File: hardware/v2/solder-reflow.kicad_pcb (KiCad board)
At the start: 2 copper layers, 108 parts, among them J1 USB_C_Receptacle_USB2.0_14P, J11 I2C, J13 RTD_PT100, J14 SSROUT2, J15 LCD_CONN, J16 UART, J17 USB_C_Receptacle_USB2.0_14P, J2 I2S, J3 PINOUT, J4 220V, J5 HEATER, J6 InputButton, J7 PINOUT, J8 PINOUT, J9 12VIN, K1 G3MB202PDC12, Q1 SS8550, Q2 SS8550, Q3 SS8050, Q4 SS8050, SW1 L, SW2 RST, SW3 SWH11AA1, SW4 D, SW5 U, SW6 R, SW7 R, SW8 R, SW9 Boot, U3 L7805, U4 AMS1117-3.3, U5 ESP32-S3-WROOM-1, U6 74LS14, U7 H11AA1, U8 CH340C, U9 MAX31865xTP

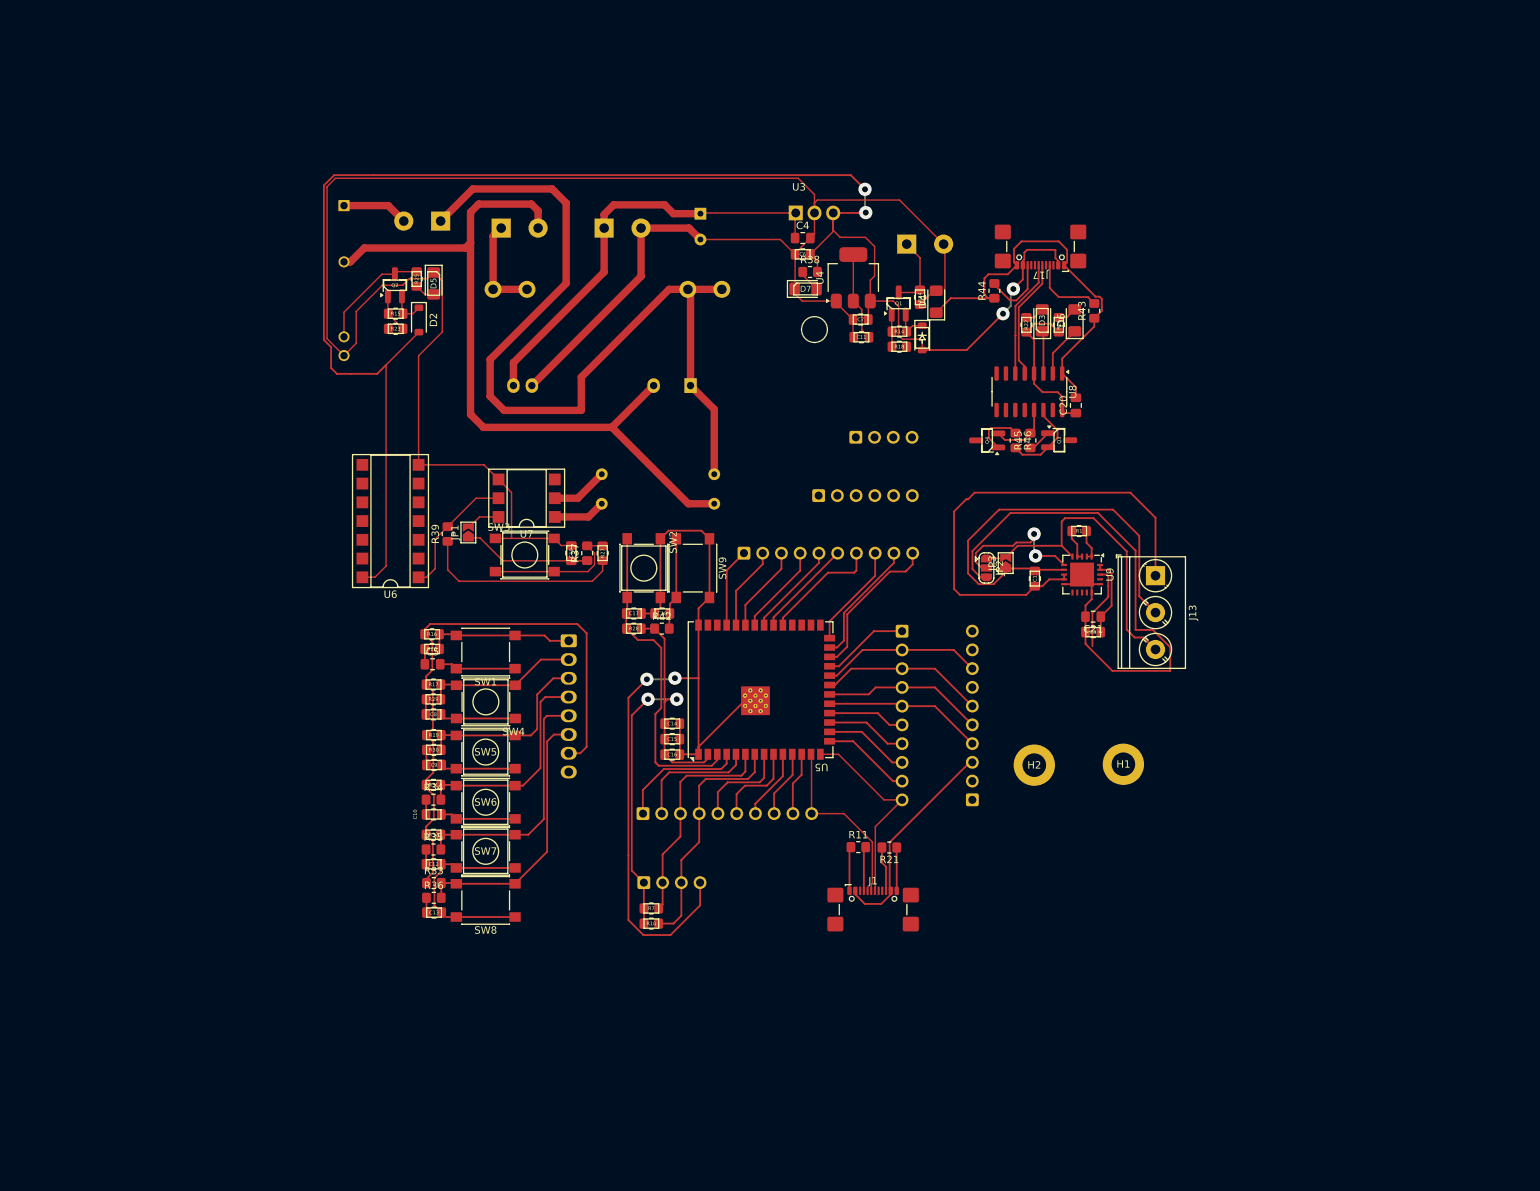
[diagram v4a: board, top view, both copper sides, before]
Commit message: feat: change to use esp32-s3 tempel
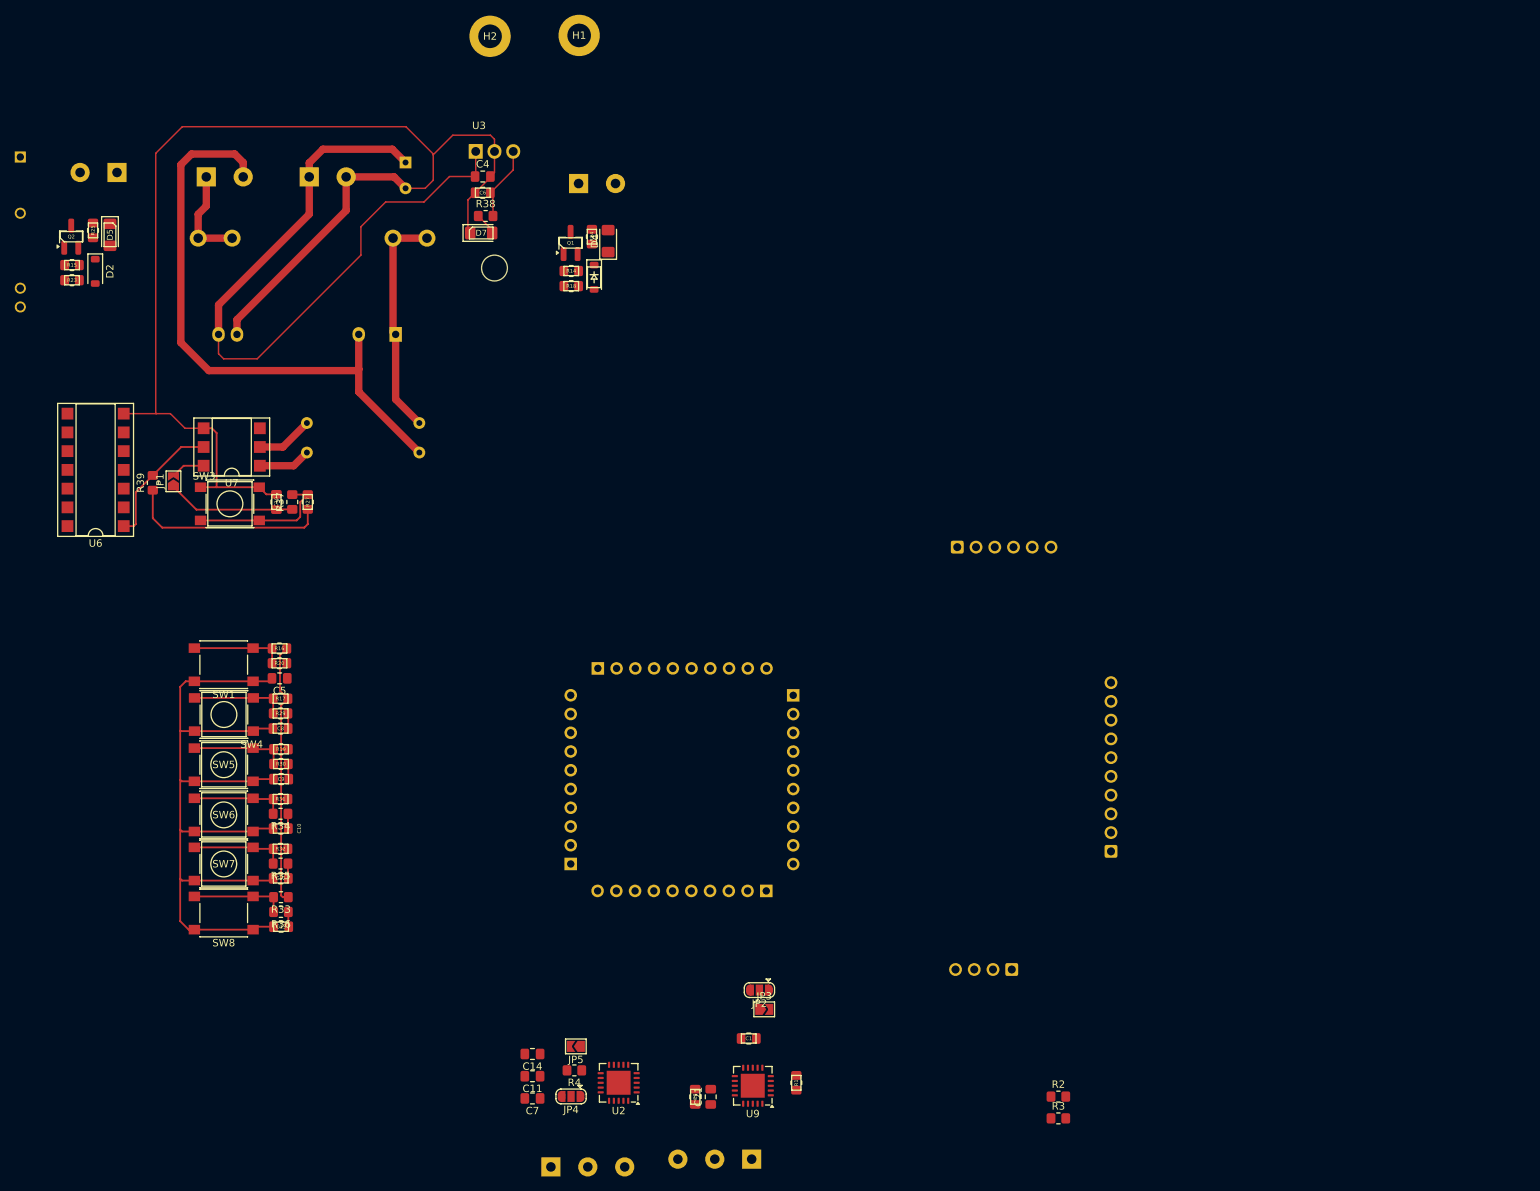
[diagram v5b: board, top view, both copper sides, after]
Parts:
- removed C15: 22uF, Capacitor_SMD:C_0805_2012Metric_Pad1.18x1.45mm_HandSolder
- removed C16: 1uF, Capacitor_SMD:C_0805_2012Metric_Pad1.18x1.45mm_HandSolder
- removed C17, C18, C20: 100nF, Capacitor_SMD:C_0805_2012Metric_Pad1.18x1.45mm_HandSolder
- removed D3: TXD, LED_SMD:LED_1206_3216Metric_Pad1.42x1.75mm_HandSolder
- removed D6: RXD, LED_SMD:LED_1206_3216Metric_Pad1.42x1.75mm_HandSolder
- removed J11: I2C, Connector_Molex:Molex_SL_171971-0004_1x04_P2.54mm_Vertical
- removed J16: UART, Connector_Molex:Molex_SL_171971-0004_1x04_P2.54mm_Vertical
- removed J17: USB_C_Receptacle_USB2.0_14P, Connector_USB:USB_C_Receptacle_GCT_USB4110
- removed J6: InputButton, Connector_Molex:Molex_KK-254_AE-6410-08A_1x08_P2.54mm_Vertical
- removed J7, J8: PINOUT, Connector_Molex:Molex_SL_171971-0010_1x10_P2.54mm_Vertical
- removed Q3, Q4: SS8050, Package_TO_SOT_SMD:SOT-23_Handsoldering
- removed R10, R7: 4K7, Resistor_SMD:R_0805_2012Metric_Pad1.20x1.40mm_HandSolder
- removed R11, R21, R43, R44: 5K1, Resistor_SMD:R_0805_2012Metric_Pad1.20x1.40mm_HandSolder
- removed R22, R26, R28, R42: 1k, Resistor_SMD:R_0805_2012Metric_Pad1.20x1.40mm_HandSolder
- removed R45, R46: 10k, Resistor_SMD:R_0805_2012Metric_Pad1.20x1.40mm_HandSolder
- removed SW2: RST, Button_Switch_SMD:SW_Push_1P1T_NO_6x6mm_H9.5mm
- removed SW9: Boot, Button_Switch_SMD:SW_Push_1P1T_NO_6x6mm_H9.5mm
- removed U4: AMS1117-3.3, Package_TO_SOT_SMD:SOT-223-3_TabPin2
- removed U5: ESP32-S3-WROOM-1, RF_Module:ESP32-S3-WROOM-1U
- removed U8: CH340C, Package_SO:SOIC-16_3.9x9.9mm_P1.27mm
- added JP4: 3_OR_2_Wire, Jumper:SolderJumper-3_P1.3mm_Open_RoundedPad1.0x1.5mm, F.Cu at (102.6, 164.9)
- added JP5: 2_Wire, Jumper:SolderJumper-2_P1.3mm_Open_TrianglePad1.0x1.5mm, F.Cu at (103.3, 158.1)
- added R2: 4K7, Resistor_SMD:R_0805_2012Metric_Pad1.20x1.40mm_HandSolder, F.Cu at (168.6, 164.9)
- added R3: 4K7, Resistor_SMD:R_0805_2012Metric_Pad1.20x1.40mm_HandSolder, F.Cu at (168.6, 167.8)
- added R4: 400 1%, Resistor_SMD:R_0805_2012Metric_Pad1.20x1.40mm_HandSolder, F.Cu at (103.1, 161.3)
- added U1: ESP32-S3-Tempel, esp32-s3-tempel-lib:esp32-s3-tempel, B.Cu at (117.2, 102.9)
- added U2: MAX31865xTP, Package_DFN_QFN:TQFN-20-1EP_5x5mm_P0.65mm_EP3.25x3.25mm, F.Cu at (109.1, 163.0)
- C11, C7: value 22uF -> 100nF
- J1: value USB_C_Receptacle_USB2.0_14P -> I2C; footprint Connector_USB:USB_C_Receptacle_GCT_USB4110 -> Connector_Molex:Molex_SL_171971-0004_1x04_P2.54mm_Vertical; moved to B.Cu
- J13: moved to B.Cu
- J3: value PINOUT -> RTD_PT100; footprint Connector_Molex:Molex_SL_171971-0010_1x10_P2.54mm_Vertical -> TerminalBlock_Phoenix:TerminalBlock_Phoenix_PT-1,5-3-5.0-H_1x03_P5.00mm_Horizontal
- moved H2 123.3 mm to (91.6, 21.2)
- moved H1 123.3 mm to (103.7, 21.1)
- moved C7 114.5 mm to (97.4, 165.1)
- moved C11 109.6 mm to (97.4, 162.1)
- moved J13 96.2 mm to (127.1, 173.4), turned to 180 degrees
- moved R1 84.0 mm to (133.1, 163.0), turned to 90 degrees
- moved C21 83.2 mm to (121.5, 164.9), turned to 90 degrees
- moved C3 82.9 mm to (119.4, 164.9), turned to 90 degrees
- moved U9 82.4 mm to (127.2, 163.4), turned to 180 degrees
- moved C1 73.4 mm to (126.7, 157.0), turned to 180 degrees
- moved JP3 68.7 mm to (128.8, 153.1), turned to 0 degrees
- moved JP2 65.0 mm to (128.1, 150.5), turned to 180 degrees
- moved J3 49.5 mm to (99.9, 174.4)
- moved C14 48.6 mm to (97.4, 159.1), turned to 180 degrees
- moved D4 45.2 mm to (107.6, 49.0)
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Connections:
- C14 pad 1: +3.3V -> Net-(J3-Pin_2)
- C14 pad 2: GND -> Net-(J3-Pin_1)
- C7 pad 1: +5V -> +3.3V
- J3 pad 1: /PT100 -> Net-(J3-Pin_1)
- J3 pad 2: /IO5 -> Net-(J3-Pin_2)
- J3 pad 3: /I2C_SDA -> Net-(J3-Pin_3)
- U9 pad 13: /IO8 -> /IO5
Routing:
- net GND: track 610.8 -> 284.7 mm, vias 2 -> 0
- net +5V: track 252.9 -> 10.2 mm, vias 4 -> 0
- net +3.3V: track 215.2 -> 66.2 mm, vias 2 -> 0
- net LINE: track 118.2 -> 31.1 mm
- net Net-(J13-Pin_1): track 64.9 -> 0.00 mm
- net Net-(J13-Pin_2): track 57.2 -> 0.00 mm
- net /EN: track 43.6 -> 0.00 mm
- net Net-(J13-Pin_3): track 42.7 -> 0.00 mm
- net +12V: track 58.8 -> 96.5 mm
- net /I2C_SCL: track 32.6 -> 0.00 mm
- net /I2C_SDA: track 29.9 -> 0.00 mm
- net /IO5: track 28.4 -> 0.00 mm
- net /USB_D+: track 27.5 -> 0.00 mm
- net /USB_D-: track 24.3 -> 0.00 mm
- net /sw6: track 36.5 -> 12.8 mm
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
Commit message: feat: finish routing v3 prototype 1
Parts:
- removed C11, C14, C7: 100nF, Capacitor_SMD:C_0805_2012Metric_Pad1.18x1.45mm_HandSolder
- removed J3: RTD_PT100, TerminalBlock_Phoenix:TerminalBlock_Phoenix_PT-1,5-3-5.0-H_1x03_P5.00mm_Horizontal
- removed JP4: 3_OR_2_Wire, Jumper:SolderJumper-3_P1.3mm_Open_RoundedPad1.0x1.5mm
- removed JP5: 2_Wire, Jumper:SolderJumper-2_P1.3mm_Open_TrianglePad1.0x1.5mm
- removed R4: 400 1%, Resistor_SMD:R_0805_2012Metric_Pad1.20x1.40mm_HandSolder
- removed U2: MAX31865xTP, Package_DFN_QFN:TQFN-20-1EP_5x5mm_P0.65mm_EP3.25x3.25mm
- added H3: MountingHole_Pad, MountingHole:MountingHole_3.2mm_M3_DIN965_Pad, F.Cu at (74.8, 118.2)
- added H4: MountingHole_Pad, MountingHole:MountingHole_3.2mm_M3_DIN965_Pad, F.Cu at (225.0, 118.7)
- SW1, SW4, SW5, SW6, SW7, SW8: footprint Button_Switch_SMD:SW_Push_1P1T_NO_6x6mm_H9.5mm -> Button_Switch_SMD:SW_Push_1P1T_NO_CK_KMR2
- moved SW1 151.2 mm to (206.5, 115.4), turned to -90 degrees
- moved C5 145.0 mm to (208.1, 110.0), turned to -90 degrees
- moved SW4 144.8 mm to (200.3, 115.5), turned to -90 degrees
- moved R20 143.0 mm to (206.1, 110.0), turned to -90 degrees
- moved R16 141.1 mm to (204.1, 110.0), turned to -90 degrees
- moved SW6 139.2 mm to (194.3, 115.5), turned to -90 degrees
- moved C8 138.8 mm to (202.0, 110.0), turned to -90 degrees
- moved R29 136.7 mm to (200.0, 110.0), turned to -90 degrees
- moved R17 134.7 mm to (198.0, 110.0), turned to -90 degrees
- moved C10 133.9 mm to (195.9, 110.0), turned to -90 degrees
- moved SW7 133.8 mm to (188.1, 115.5), turned to -90 degrees
- moved R34 131.7 mm to (193.9, 110.0), turned to -90 degrees
- moved R31 129.5 mm to (191.9, 110.0), turned to -90 degrees
- moved C12 129.1 mm to (189.8, 110.0), turned to -90 degrees
- moved SW8 128.9 mm to (182.1, 115.5), turned to -90 degrees
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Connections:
- net /MTDI renamed /IO41
- U1 pad 29: /MTMS -> /IO42
- U9 pad 18: /IO5 -> /IO42
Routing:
- net GND: track 284.7 -> 635.9 mm
- net +5V: track 10.2 -> 279.2 mm, vias 0 -> 4
- net +3.3V: track 66.2 -> 304.8 mm, vias 0 -> 4
- net /SSRIN1: track 0.00 -> 226.8 mm, vias 0 -> 2
- net /IO42: track 0.00 -> 115.1 mm, vias 0 -> 4
- net /ZC_INPUT: track 0.00 -> 110.8 mm, vias 0 -> 2
- net /IO5: track 0.00 -> 101.5 mm, vias 0 -> 4
- net LINE: track 31.1 -> 111.9 mm
- net /SSRIN2: track 0.00 -> 77.9 mm, vias 0 -> 2
- net /I2C_SCL: track 0.00 -> 58.3 mm
- net /IO8: track 0.00 -> 52.7 mm
- net /QUADHD: track 0.00 -> 44.8 mm
- net Net-(JP2-C): track 0.00 -> 39.0 mm, vias 0 -> 2
- net NEUT: track 80.8 -> 119.3 mm
- net /IN6: track 2.03 -> 40.4 mm
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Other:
- board outline added: 163.5 x 80.3 mm
- board text added: "Blendingen"
- board text added: "SORE"

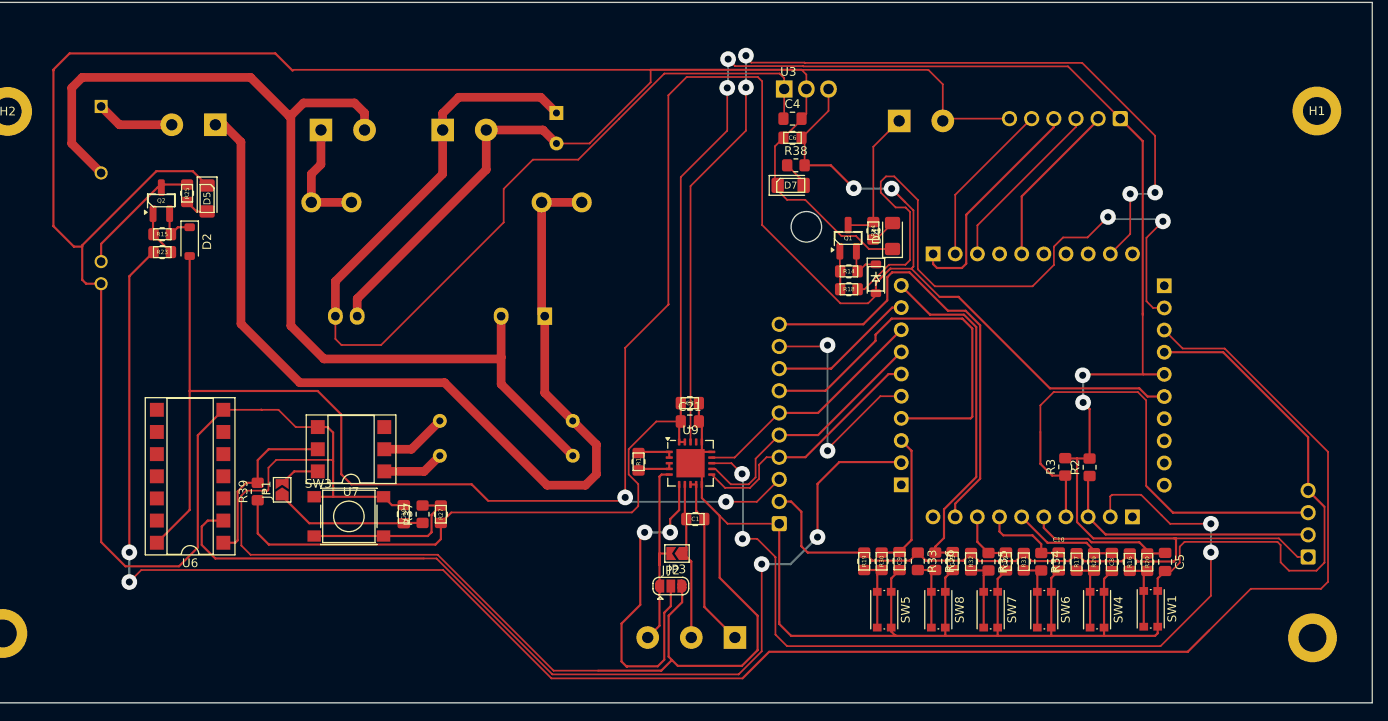
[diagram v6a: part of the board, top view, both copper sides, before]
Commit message: feat: update schematic svg
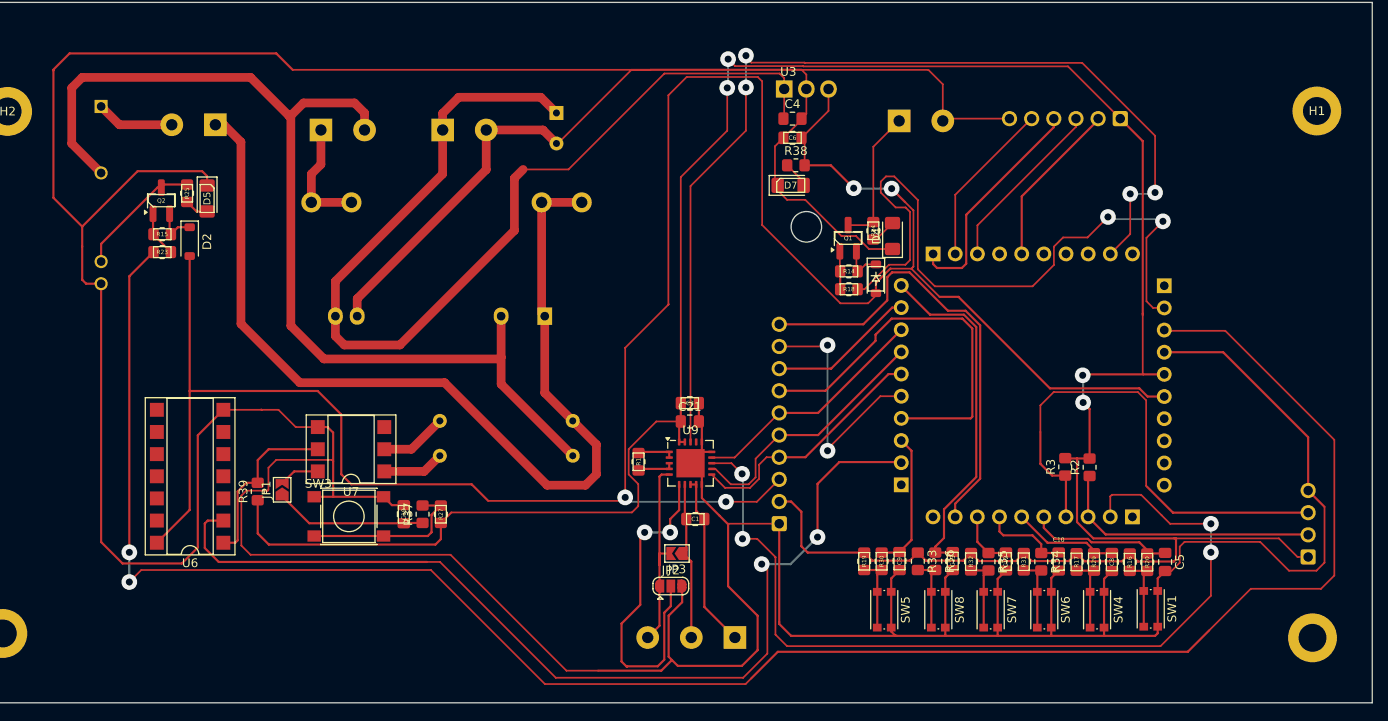
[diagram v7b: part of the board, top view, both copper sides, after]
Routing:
- net GND: track 635.9 -> 631.2 mm
- net /SSRIN1: track 226.8 -> 229.2 mm
- net +12V: track 117.3 -> 118.4 mm
- net /ZC_INPUT: track 110.8 -> 111.9 mm

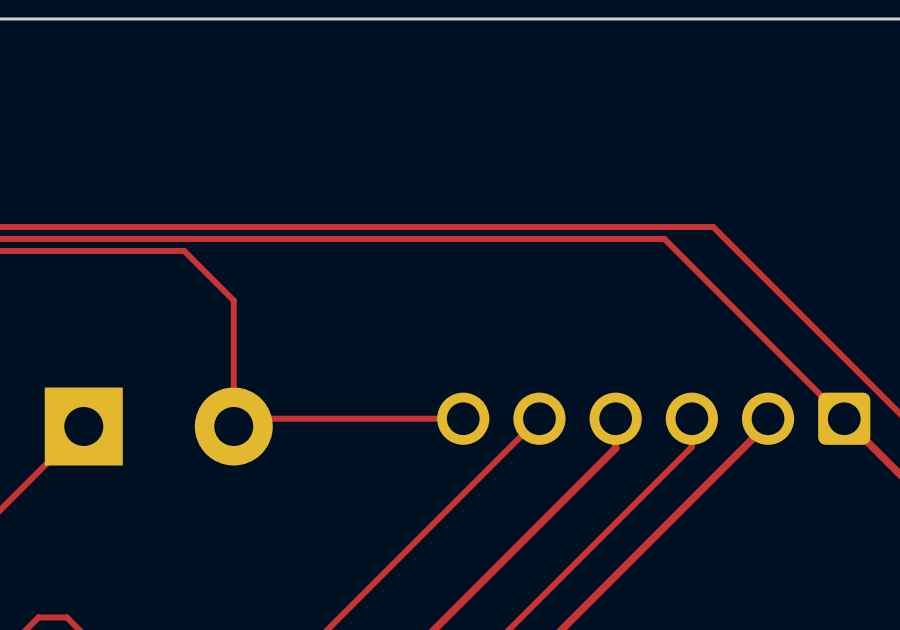
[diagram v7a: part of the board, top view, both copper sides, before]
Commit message: feat: add led indicator
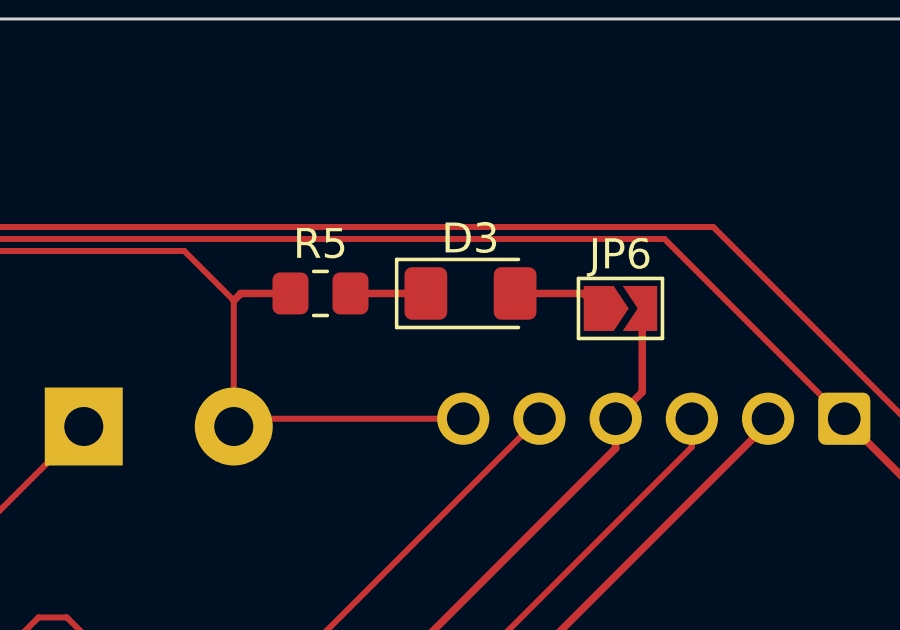
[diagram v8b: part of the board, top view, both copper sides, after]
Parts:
- added D3: Indicator, LED_SMD:LED_1206_3216Metric_Pad1.42x1.75mm_HandSolder, F.Cu at (190.5, 55.0)
- added JP6: 2_Wire, Jumper:SolderJumper-2_P1.3mm_Open_TrianglePad1.0x1.5mm, F.Cu at (195.5, 55.5)
- added R5: 1K, Resistor_SMD:R_0805_2012Metric_Pad1.20x1.40mm_HandSolder, F.Cu at (185.5, 55.0)
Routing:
- net /WS: track 26.1 -> 30.2 mm
- net Net-(D3-A): track 0.00 -> 2.99 mm
- net Net-(D3-K): track 0.00 -> 2.51 mm
- net GND: track 631.2 -> 633.2 mm
